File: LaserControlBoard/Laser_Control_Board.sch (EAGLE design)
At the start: 32 parts, among them J1 Servo Header, J2 FTDI Header, J5 FEMALE 2x3, U1 ATMEGA328P_TQFP, Y1 16MHz

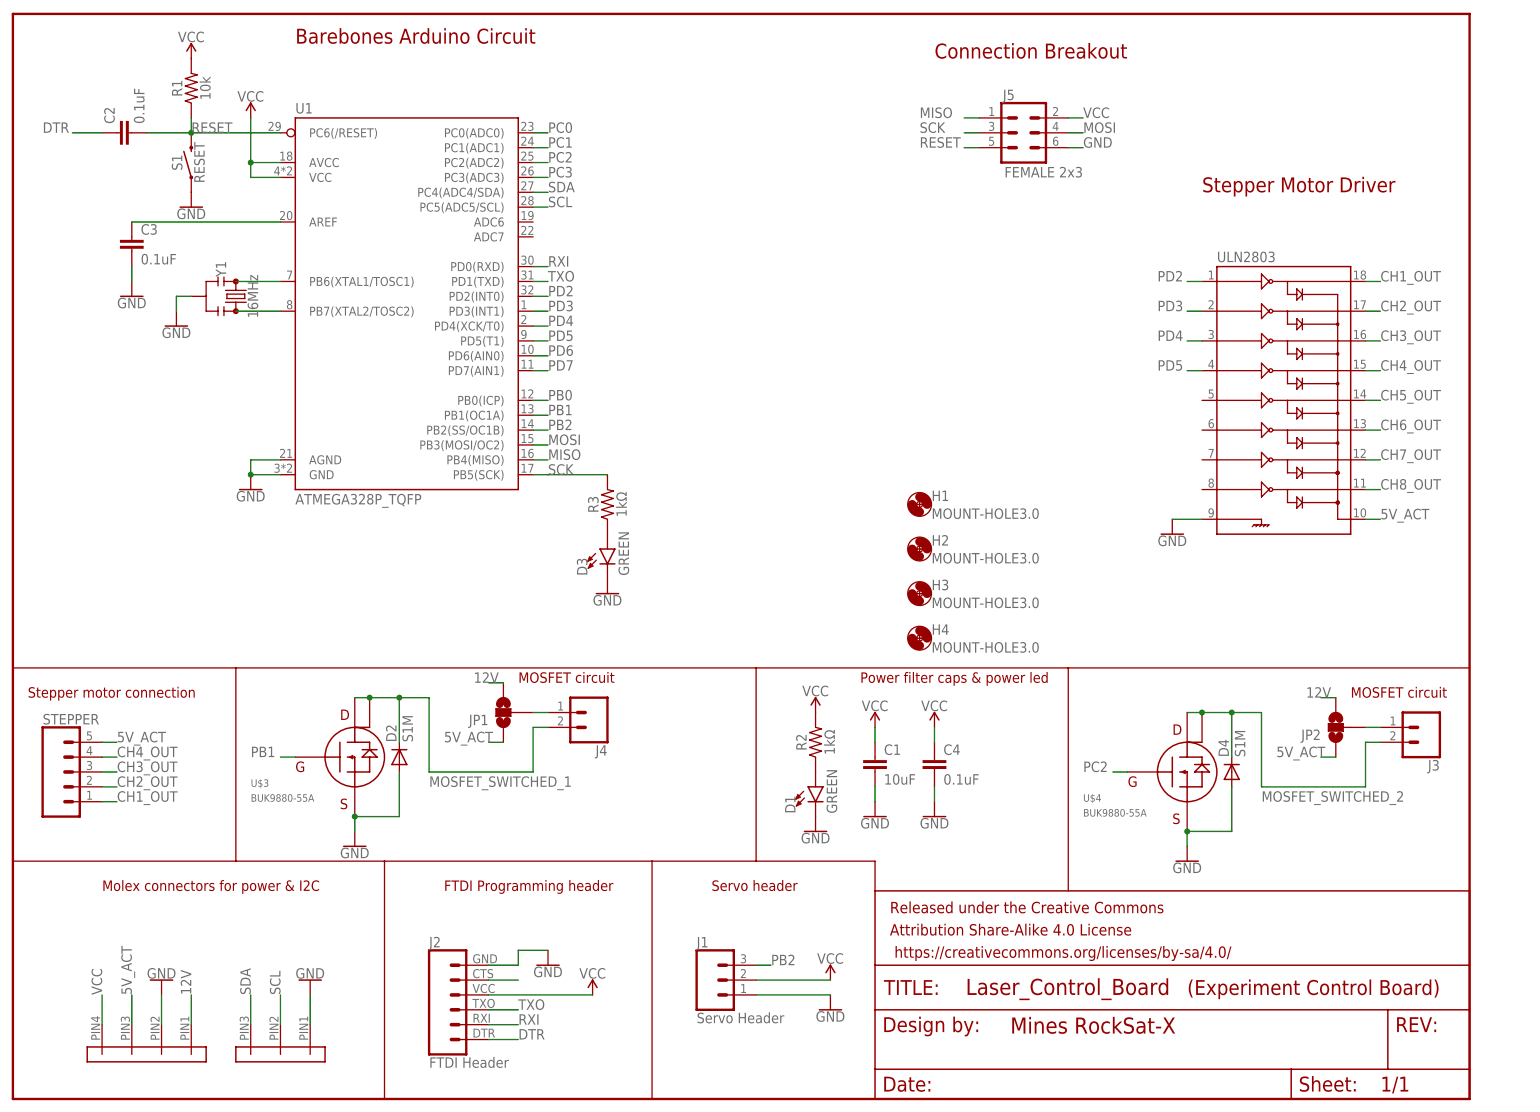
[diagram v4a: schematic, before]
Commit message: Breakout headers added to Experiment Control board.
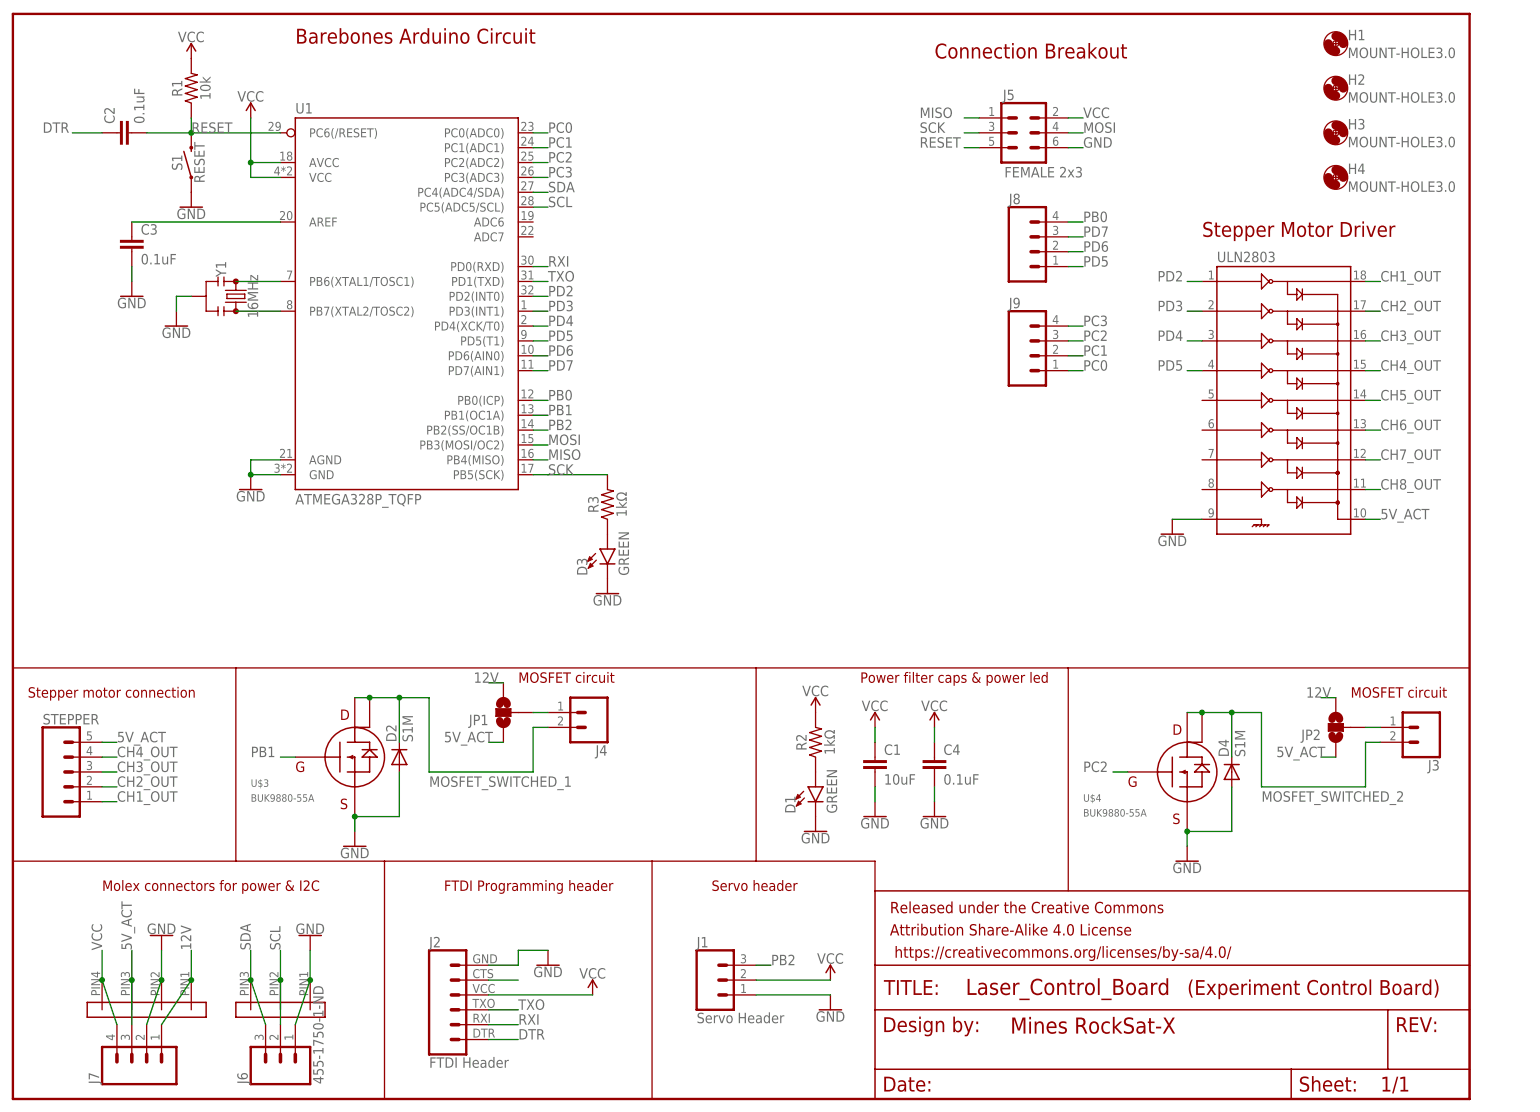
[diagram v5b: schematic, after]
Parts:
- added J6: 455-1750-1-ND, SparkFun-Connectors:CONN_03
- added J7, J8, J9: (no value), SparkFun-Connectors:CONN_04LOCK
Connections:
- net 12V: now also J7.1
- net 5V_ACT: now also J7.3
- net GND: now also J6.1, J7.2
- net PB0: now also J8.4
- net PC0: now also J9.1
- net PC1: now also J9.2
- net PC2: now also J9.3
- net PC3: now also J9.4
- net PD5: now also J8.1
- net PD6: now also J8.2
- net PD7: now also J8.3
- net SCL: now also J6.2
- net SDA: now also J6.3
- net VCC: now also J7.4
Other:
- moved on the sheet: H1, H2, H3, H4

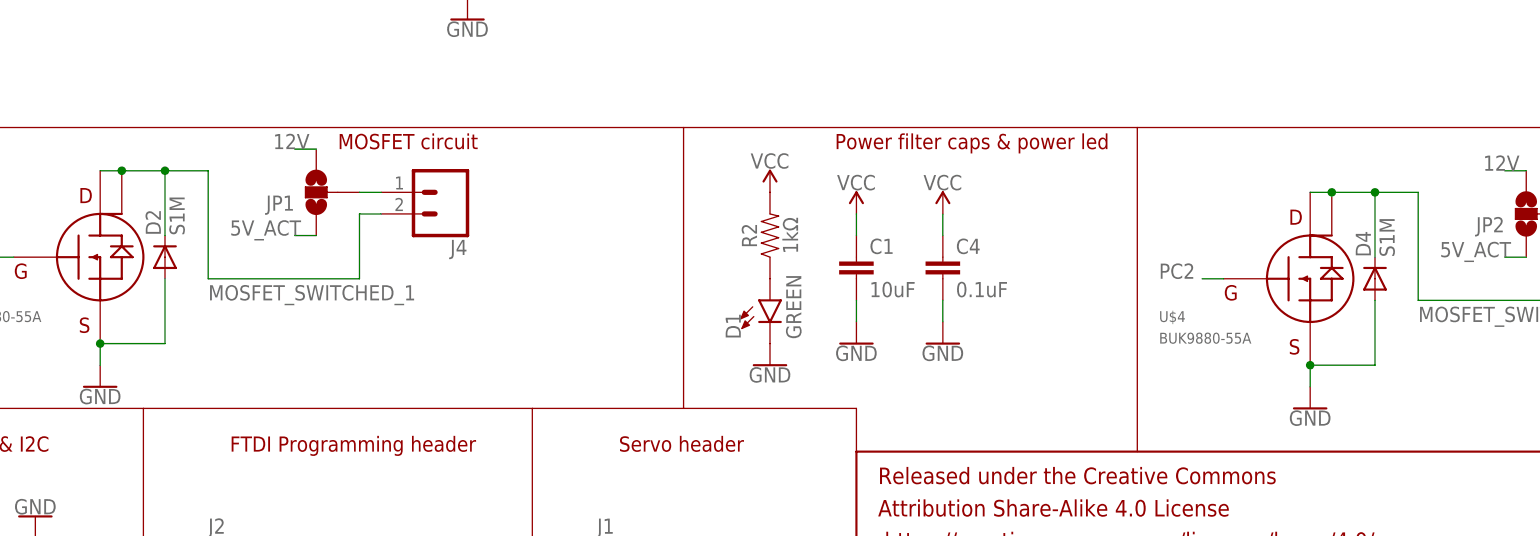
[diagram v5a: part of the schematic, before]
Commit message: Improved Molex connector footprints.
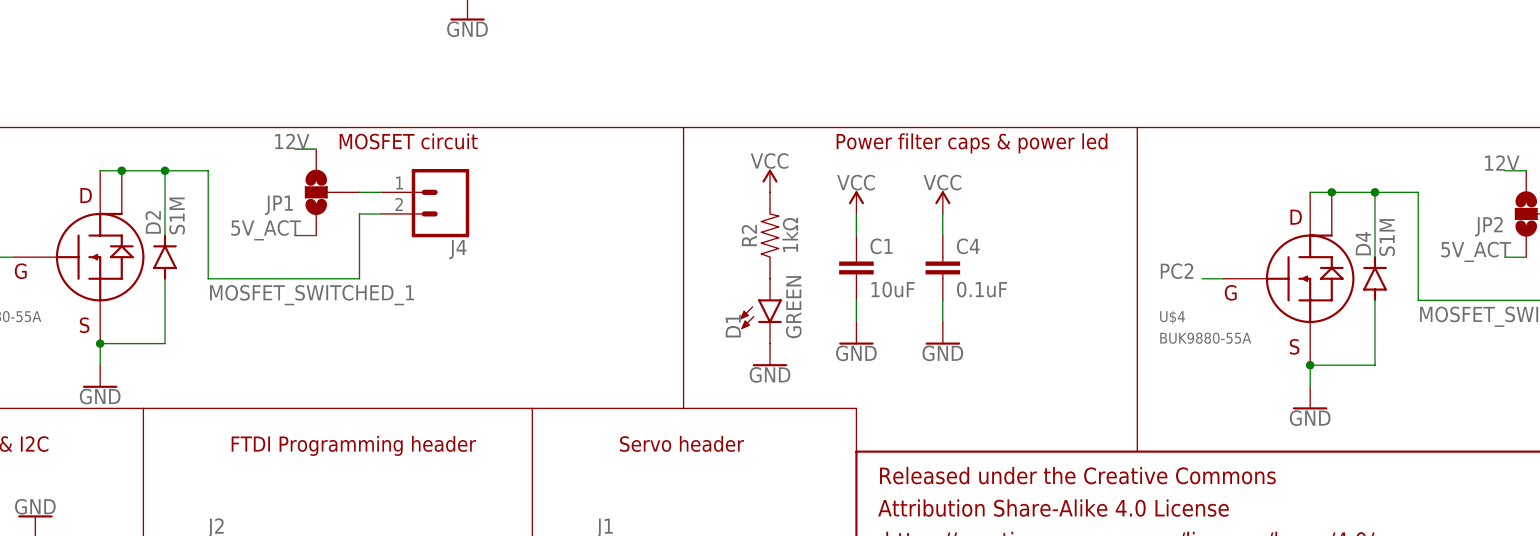
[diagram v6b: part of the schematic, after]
